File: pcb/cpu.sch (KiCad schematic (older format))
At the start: 132 parts, among them J1 Conn_02x16_Counter_Clockwise, J2 Conn_01x16, U1 74LS283, U2 74LS283, U3 74LS283, U4 74LS283

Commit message: ti registers
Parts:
- removed U?: 74FCT163374APAG8, symbol nand2tetris:74FCT163374APAG8
- added Register_A, Register_D: SN74LVCH16374A, symbol nand2tetris:SN74LVCH16374A
- added U? (x2): 74LS08, symbol 74xx:74LS08
- gave numbers to parts that had none: 1
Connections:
- net labels added: ar0, ar1, ar10, ar11, ar12, ar13, ar14, ar15, ar2, ar3, ar4, ar5, ar6, ar7, ar8, ar9, clk, la, ld
- wire segments 612 -> 654
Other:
- moved on the sheet: U?

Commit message: instruction decoder and program counter
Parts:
- removed Register_A, Register_D: SN74LVCH16374A, symbol nand2tetris:SN74LVCH16374A
- removed U? (x2): 74LS08, symbol 74xx:74LS08

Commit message: flash mem
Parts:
- added J?: Conn_01x16, Connector_PinHeader_1.27mm:PinHeader_1x16_P1.27mm_Vertical, symbol Connector_Generic:Conn_01x16
- added U?: SN74LVCH16374A, symbol nand2tetris:SN74LVCH16374A
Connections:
- net +5V is gone; now on net VCC: U1.16 (VCC), U2.16 (VCC), U3.16 (VCC), U4.16 (VCC)
- net GND: now also U?.10 (GND), U?.15 (GND), U?.21 (GND), U?.28 (GND), U?.34 (GND), U?.39 (GND), U?.4 (GND), U?.45 (GND)
- net VCC: now also U?.18 (VCC), U?.31 (VCC), U?.42 (VCC), U?.7 (VCC)
- net addr0: now also RAM.5 (A0)
- net addr1: now also RAM.4 (A1)
- net addr10: now also RAM.25 (A10)
- net addr11: now also RAM.24 (A11)
- net addr12: now also RAM.21 (A12)
- net addr13: now also RAM.20 (A13)
- net addr14: now also RAM.19 (A14)
- net addr2: now also RAM.3 (A2)
- net addr3: now also RAM.2 (A3)
- net addr4: now also RAM.18 (A4)
- net addr5: now also RAM.44 (A5)
- net addr6: now also RAM.43 (A6)
- net addr7: now also RAM.42 (A7)
- net addr8: now also RAM.27 (A8)
- net addr9: now also RAM.26 (A9)
- net kbd0: now also J?.1 (Pin_1), U?.46 (1D1); no longer U?.0 (out)
- net kbd1: now also J?.2 (Pin_2), U?.48 (1D2); no longer U?.1 (out)
- net kbd10: now also J?.11 (Pin_11), U?.33 (2D3); no longer U?.10 (out)
- net kbd11: now also J?.12 (Pin_12), U?.32 (2D4); no longer U?.11 (out)
- net kbd12: now also J?.13 (Pin_13), U?.30 (2D5); no longer U?.12 (out)
- net kbd13: now also J?.14 (Pin_14), U?.29 (2D6); no longer U?.13 (out)
- net kbd14: now also J?.15 (Pin_15), U?.27 (2D7); no longer U?.14 (out)
- net kbd15: now also J?.16 (Pin_16), U?.26 (2D8); no longer U?.15 (out)
- net kbd2: now also J?.3 (Pin_3), U?.44 (1D3); no longer U?.2 (out)
- net kbd3: now also J?.4 (Pin_4), U?.43 (1D4); no longer U?.3 (out)
- net kbd4: now also J?.5 (Pin_5), U?.41 (1D5); no longer U?.4 (out)
- net kbd5: now also J?.6 (Pin_6), U?.40 (1D6); no longer U?.5 (out)
- net kbd6: now also J?.7 (Pin_7), U?.38 (1D7); no longer U?.6 (out)
- net kbd7: now also J?.8 (Pin_8), U?.37 (1D8); no longer U?.7 (out)
- net kbd8: now also J?.9 (Pin_9), U?.36 (2D1); no longer U?.8 (out)
- net kbd9: now also J?.10 (Pin_10), U?.35 (2D2); no longer U?.9 (out)
- net mem0: now also U?.56 (1B1)
- net mem1: now also U?.2 (2B1)
- net mem10: now also U?.39 (11B1)
- net mem11: now also U?.19 (12B1)
- net mem12: now also U?.36 (13B1)
- net mem13: now also U?.22 (14B1)
- net mem14: now also U?.33 (15B1)
- net mem15: now also U?.25 (16B1)
- net mem2: now also U?.53 (3B1)
- net mem3: now also U?.5 (4B1)
- net mem4: now also U?.50 (5B1)
- net mem5: now also U?.8 (6B1)
- net mem6: now also U?.47 (7B1)
- net mem7: now also U?.11 (8B1)
- net mem8: now also U?.42 (9B1)
- net mem9: now also U?.16 (10B1)
- net notband11: no longer U?.4
- net dr7: now reaches U?.11 (8B1)
- net dr9: now reaches U?.16 (10B1)
- net dr11: now reaches U?.19 (12B1)
- net dr1: now reaches U?.2 (2B1)
- net dr13: now reaches U?.22 (14B1)
- net dr15: now reaches U?.25 (16B1)
- net dr14: now reaches U?.33 (15B1)
- net dr12: now reaches U?.36 (13B1)
- net dr10: now reaches U?.39 (11B1)
- net dr8: now reaches U?.42 (9B1)
- net dr6: now reaches U?.47 (7B1)
- net dr3: now reaches U?.5 (4B1)
- net dr4: now reaches U?.50 (5B1)
- net dr2: now reaches U?.53 (3B1)
- net dr0: now reaches U?.56 (1B1)
- net dr5: now reaches U?.8 (6B1)
- new net clk: U?.25 (2CLK), U?.48 (1D2)
- new net high: U?.1 (1~OE~), U?.24 (2~OE~)
- new net inr0: U?.0 (out), U?.2 (1Q1)
- new net inr1: U?.1 (out), U?.3 (1Q2)
- new net inr10: U?.10 (out), U?.16 (2Q3)
- new net inr11: U?.11 (out), U?.17 (2Q4)
- new net inr12: U?.12 (out), U?.19 (2Q5)
- new net inr13: U?.13 (out), U?.20 (2Q6)
- new net inr14: U?.14 (out), U?.22 (2Q7)
- new net inr15: U?.15 (out), U?.23 (2Q8)
- new net inr2: U?.2 (out), U?.5 (1Q3)
- new net inr3: U?.3 (out), U?.6 (1Q4)
- new net inr4: U?.4 (out), U?.8 (1Q5)
- new net inr5: U?.5 (out), U?.9 (1Q6)
- new net inr6: U?.11 (1Q7), U?.6 (out)
- new net inr7: U?.12 (1Q8), U?.7 (out)
- new net inr8: U?.13 (2Q1), U?.8 (out)
- new net inr9: U?.14 (2Q2), U?.9 (out)
- new net kinr0: U?.0 (out), U?.0 (out)
- new net kinr1: U?.1 (out), U?.1 (out)
- new net kinr10: U?.10 (out), U?.10 (out)
- new net kinr11: U?.11 (out), U?.11 (out)
- new net kinr12: U?.12 (out), U?.12 (out)
- new net kinr13: U?.13 (out), U?.13 (out)
- new net kinr14: U?.14 (out), U?.14 (out)
- new net kinr15: U?.15 (out), U?.15 (out)
- new net kinr2: U?.2 (out), U?.2 (out)
- new net kinr3: U?.3 (out), U?.3 (out)
- new net kinr4: U?.4 (out), U?.4 (out)
- new net kinr5: U?.5 (out), U?.5 (out)
- new net kinr6: U?.6 (out), U?.6 (out)
- new net kinr7: U?.7 (out), U?.7 (out)
- new net kinr8: U?.8 (out), U?.8 (out)
- new net kinr9: U?.9 (out), U?.9 (out)
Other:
- moved on the sheet: U1, U2, U3, U4, U?, U?A

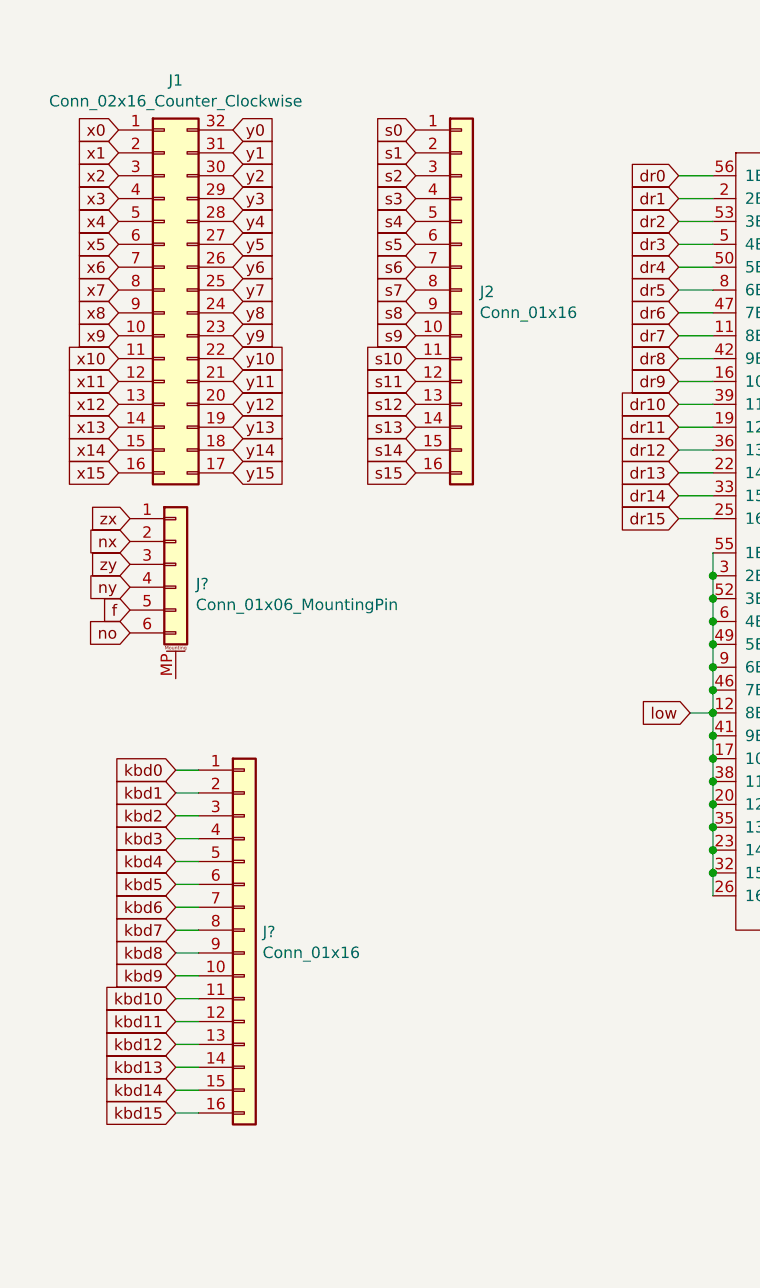
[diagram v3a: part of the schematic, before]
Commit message: delete unnecessary inputs
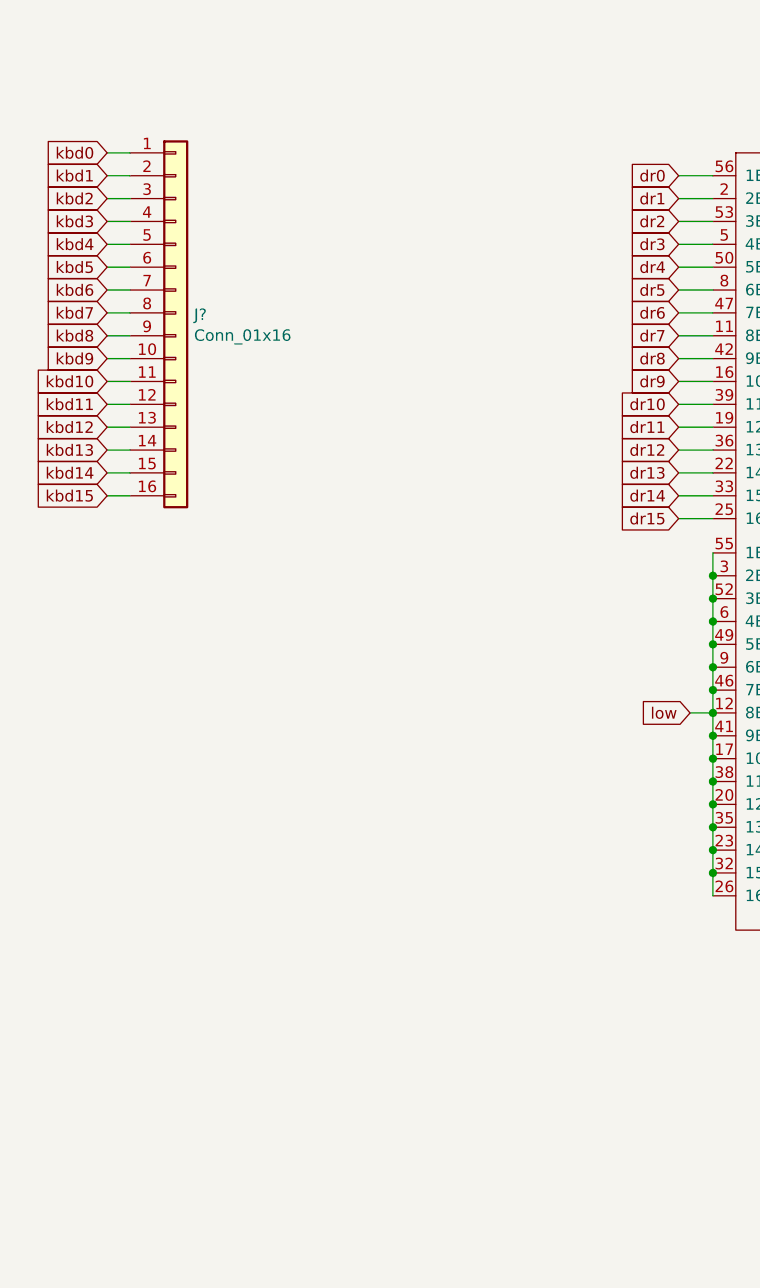
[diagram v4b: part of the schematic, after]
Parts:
- removed J1: Conn_02x16_Counter_Clockwise, Connector_PinHeader_1.27mm:PinHeader_2x16_P1.27mm_Vertical, symbol Connector_Generic:Conn_02x16_Counter_Clockwise
- removed J2: Conn_01x16, Connector_PinHeader_1.27mm:PinHeader_1x16_P1.27mm_Vertical, symbol Connector_Generic:Conn_01x16
- removed J?: Conn_01x06_MountingPin, symbol Connector_Generic_MountingPin:Conn_01x06_MountingPin
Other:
- moved on the sheet: J?
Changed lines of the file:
@@
 Comment4 ""
 $EndDescr
-Text GLabel 1450 2450 2    50   Input ~ 0
-y15
-Text GLabel 1450 2350 2    50   Input ~ 0
-y14
-Text GLabel 1450 2250 2    50   Input ~ 0
-y13
-Text GLabel 1450 2150 2    50   Input ~ 0
-y12
-Text GLabel 1450 2050 2    50   Input ~ 0
-y11
-Text GLabel 1450 1950 2    50   Input ~ 0
-y10
-Text GLabel 1450 1850 2    50   Input ~ 0
-y9
-Text GLabel 1450 1750 2    50   Input ~ 0
-y8
-Text GLabel 1450 1650 2    50   Input ~ 0
-y7
-Text GLabel 1450 1550 2    50   Input ~ 0
-y6
-Text GLabel 1450 1450 2    50   Input ~ 0
-y5
-Text GLabel 1450 1350 2    50   Input ~ 0
-y4
-Text GLabel 1450 1250 2    50   Input ~ 0
-y3
-Text GLabel 1450 1150 2    50   Input ~ 0
-y2
-Text GLabel 1450 1050 2    50   Input ~ 0
-y1
-Text GLabel 1450 950  2    50   Input ~ 0
-y0
-Text GLabel 950  2450 0    50   Input ~ 0
-x15
-Text GLabel 950  2350 0    50   Input ~ 0
-x14
-Text GLabel 950  2250 0    50   Input ~ 0
-x13
-Text GLabel 950  2150 0    50   Input ~ 0
-x12
-Text GLabel 950  2050 0    50   Input ~ 0
-x11
-Text GLabel 950  1950 0    50   Input ~ 0
-x10
-Text GLabel 950  1850 0    50   Input ~ 0
-x9
-Text GLabel 950  1750 0    50   Input ~ 0
-x8
-Text GLabel 950  1650 0    50   Input ~ 0
-x7
-Text GLabel 950  1550 0    50   Input ~ 0
-x6
-Text GLabel 950  1450 0    50   Input ~ 0
-x5
-Text GLabel 950  1350 0    50   Input ~ 0
-x4
-Text GLabel 950  1250 0    50   Input ~ 0
-x3
-Text GLabel 950  1150 0    50   Input ~ 0
-x2
-Text GLabel 950  1050 0    50   Input ~ 0
-x1
-Text GLabel 950  950  0    50   Input ~ 0
-x0
 Text GLabel 8250 2650 2    50   Input ~ 0
 opx15
@@
 	1    0    0    -1
 $EndComp
-Text GLabel 1000 3150 0    50   Input ~ 0
-no
-Text GLabel 1000 3050 0    50   Input ~ 0
-f
-Text GLabel 1000 2950 0    50   Input ~ 0
-ny
-Text GLabel 1000 2850 0    50   Input ~ 0
-zy
-Text GLabel 1000 2750 0    50   Input ~ 0
-nx
-Text GLabel 1000 2650 0    50   Input ~ 0
-zx
-$Comp
-L Connector_Generic_MountingPin:Conn_01x06_MountingPin J?
-U 1 1 5CBA2E88
-P 1200 2850
-F 0 "J?" H 1288 2764 50  0000 L CNN
-F 1 "Conn_01x06_MountingPin" H 1288 2673 50  0000 L CNN
-F 2 "" H 1200 2850 50  0001 C CNN
-F 3 "~" H 1200 2850 50  0001 C CNN
-	1    1200 2850
-	1    0    0    -1
-$EndComp
 Text GLabel 15000 1600 0    50   Input ~ 0
 opx0
@@
 Text GLabel 15000 2400 0    50   Input ~ 0
 opy3
-Text GLabel 2250 2450 0    50   Input ~ 0
-s15
-Text GLabel 2250 2350 0    50   Input ~ 0
-s14
-Text GLabel 2250 2250 0    50   Input ~ 0
-s13
-Text GLabel 2250 2150 0    50   Input ~ 0
-s12
-Text GLabel 2250 2050 0    50   Input ~ 0
-s11
-Text GLabel 2250 1950 0    50   Input ~ 0
-s10
-Text GLabel 2250 1850 0    50   Input ~ 0
-s9
-Text GLabel 2250 1750 0    50   Input ~ 0
-s8
-Text GLabel 2250 1650 0    50   Input ~ 0
-s7
-Text GLabel 2250 1550 0    50   Input ~ 0
-s6
-Text GLabel 2250 1450 0    50   Input ~ 0
-s5
-Text GLabel 2250 1350 0    50   Input ~ 0
-s4
-Text GLabel 2250 1250 0    50   Input ~ 0
-s3
-Text GLabel 2250 1150 0    50   Input ~ 0
-s2
-Text GLabel 2250 1050 0    50   Input ~ 0
-s1
-Text GLabel 2250 950  0    50   Input ~ 0
-s0
-$Comp
-L Connector_Generic:Conn_01x16 J2
-U 1 1 5CADB34A
-P 2450 1650
-F 0 "J2" H 2530 1642 50  0000 L CNN
-F 1 "Conn_01x16" H 2530 1551 50  0000 L CNN
-F 2 "Connector_PinHeader_1.27mm:PinHeader_1x16_P1.27mm_Vertical" H 2450 1650 50  0001 C CNN
-F 3 "~" H 2450 1650 50  0001 C CNN
-	1    2450 1650
-	1    0    0    -1
-$EndComp
-$Comp
-L Connector_Generic:Conn_02x16_Counter_Clockwise J1
-U 1 1 5CAD3D15
-P 1150 1650
-F 0 "J1" H 1200 2567 50  0000 C CNN
-F 1 "Conn_02x16_Counter_Clockwise" H 1200 2476 50  0000 C CNN
-F 2 "Connector_PinHeader_1.27mm:PinHeader_2x16_P1.27mm_Vertical" H 1150 1650 50  0001 C CNN
-F 3 "~" H 1150 1650 50  0001 C CNN
-	1    1150 1650
-	1    0    0    -1
-$EndComp
 NoConn ~ 22400 1900
 Text GLabel 22500 1700 2    50   Input ~ 0
@@
 L Connector_Generic:Conn_01x16 J?
 U 1 1 5DCAA822
-P 1500 4450
-F 0 "J?" H 1580 4442 50  0000 L CNN
-F 1 "Conn_01x16" H 1580 4351 50  0000 L CNN
-F 2 "Connector_PinHeader_1.27mm:PinHeader_1x16_P1.27mm_Vertical" H 1500 4450 50  0001 C CNN
-F 3 "~" H 1500 4450 50  0001 C CNN
-	1    1500 4450
+P 1200 1750
+F 0 "J?" H 1280 1742 50  0000 L CNN
+F 1 "Conn_01x16" H 1280 1651 50  0000 L CNN
+F 2 "Connector_PinHeader_1.27mm:PinHeader_1x16_P1.27mm_Vertical" H 1200 1750 50  0001 C CNN
+F 3 "~" H 1200 1750 50  0001 C CNN
+	1    1200 1750
 	1    0    0    -1
 $EndComp
@@
 Text Label 14100 13350 0    50   ~ 0
 kinr15
-Text GLabel 1200 3750 0    50   Input ~ 0
+Text GLabel 900  1050 0    50   Input ~ 0
 kbd0
-Text GLabel 1200 3850 0    50   Input ~ 0
+Text GLabel 900  1150 0    50   Input ~ 0
 kbd1
-Text GLabel 1200 3950 0    50   Input ~ 0
+Text GLabel 900  1250 0    50   Input ~ 0
 kbd2
-Text GLabel 1200 4050 0    50   Input ~ 0
+Text GLabel 900  1350 0    50   Input ~ 0
 kbd3
-Text GLabel 1200 4150 0    50   Input ~ 0
+Text GLabel 900  1450 0    50   Input ~ 0
 kbd4
-Text GLabel 1200 4250 0    50   Input ~ 0
+Text GLabel 900  1550 0    50   Input ~ 0
 kbd5
-Text GLabel 1200 4350 0    50   Input ~ 0
+Text GLabel 900  1650 0    50   Input ~ 0
 kbd6
-Text GLabel 1200 4450 0    50   Input ~ 0
+Text GLabel 900  1750 0    50   Input ~ 0
 kbd7
-Text GLabel 1200 4550 0    50   Input ~ 0
+Text GLabel 900  1850 0    50   Input ~ 0
 kbd8
-Text GLabel 1200 4650 0    50   Input ~ 0
+Text GLabel 900  1950 0    50   Input ~ 0
 kbd9
-Text GLabel 1200 4750 0    50   Input ~ 0
+Text GLabel 900  2050 0    50   Input ~ 0
 kbd10
-Text GLabel 1200 4850 0    50   Input ~ 0
+Text GLabel 900  2150 0    50   Input ~ 0
 kbd11
-Text GLabel 1200 4950 0    50   Input ~ 0
+Text GLabel 900  2250 0    50   Input ~ 0
 kbd12
-Text GLabel 1200 5050 0    50   Input ~ 0
+Text GLabel 900  2350 0    50   Input ~ 0
 kbd13
-Text GLabel 1200 5150 0    50   Input ~ 0
+Text GLabel 900  2450 0    50   Input ~ 0
 kbd14
-Text GLabel 1200 5250 0    50   Input ~ 0
+Text GLabel 900  2550 0    50   Input ~ 0
 kbd15
 Text GLabel 6350 10750 0    50   Input ~ 0
@@
 	1100 14450 1200 14450
 Wire Wire Line
-	1200 3750 1300 3750
+	900  1050 1000 1050
 Wire Wire Line
-	1200 3850 1300 3850
+	900  1150 1000 1150
 Wire Wire Line
-	1200 3950 1300 3950
+	900  1250 1000 1250
 Wire Wire Line
-	1200 4050 1300 4050
+	900  1350 1000 1350
 Wire Wire Line
-	1200 4150 1300 4150
+	900  1450 1000 1450
 Wire Wire Line
-	1200 4250 1300 4250
+	900  1550 1000 1550
 Wire Wire Line
-	1200 4350 1300 4350
+	900  1650 1000 1650
 Wire Wire Line
-	1200 4450 1300 4450
+	900  1750 1000 1750
 Wire Wire Line
-	1200 4550 1300 4550
+	900  1850 1000 1850
 Wire Wire Line
-	1200 4650 1300 4650
+	900  1950 1000 1950
 Wire Wire Line
-	1200 4750 1300 4750
+	900  2050 1000 2050
 Wire Wire Line
-	1200 4850 1300 4850
+	900  2150 1000 2150
 Wire Wire Line
-	1200 4950 1300 4950
+	900  2250 1000 2250
 Wire Wire Line
-	1200 5050 1300 5050
+	900  2350 1000 2350
 Wire Wire Line
-	1200 5150 1300 5150
+	900  2450 1000 2450
 Wire Wire Line
-	1200 5250 1300 5250
+	900  2550 1000 2550
 Wire Wire Line
 	8150 1150 8250 1150
